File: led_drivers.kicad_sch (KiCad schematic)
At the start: 23 parts, among them IC1 SamacSys_Parts_HT16K33-28SOP, IC2 SamacSys_Parts_HT16K33-28SOP, SW1 SW_Alps_SKRK, SW2 SW_Alps_SKRK, SW3 SW_Omron_B3FS, SW4 SW_Alps_SKRK

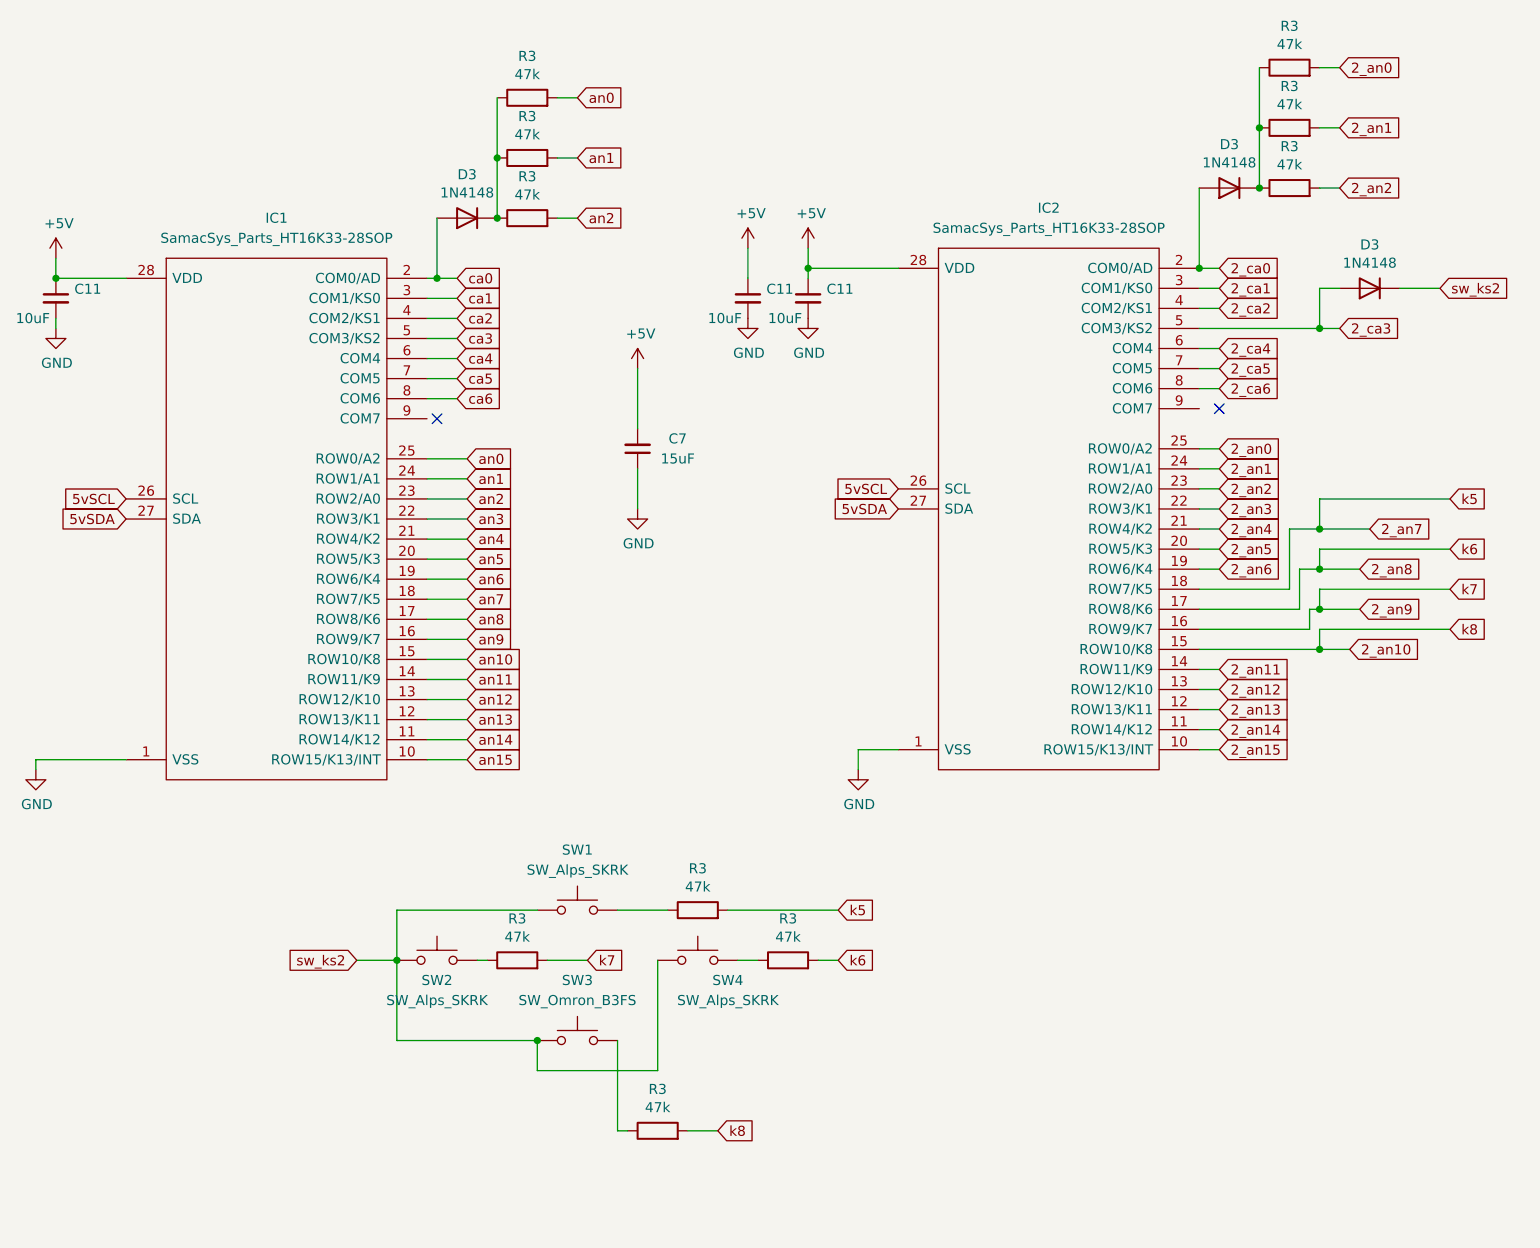
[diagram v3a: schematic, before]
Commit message: Change tactile shwitches
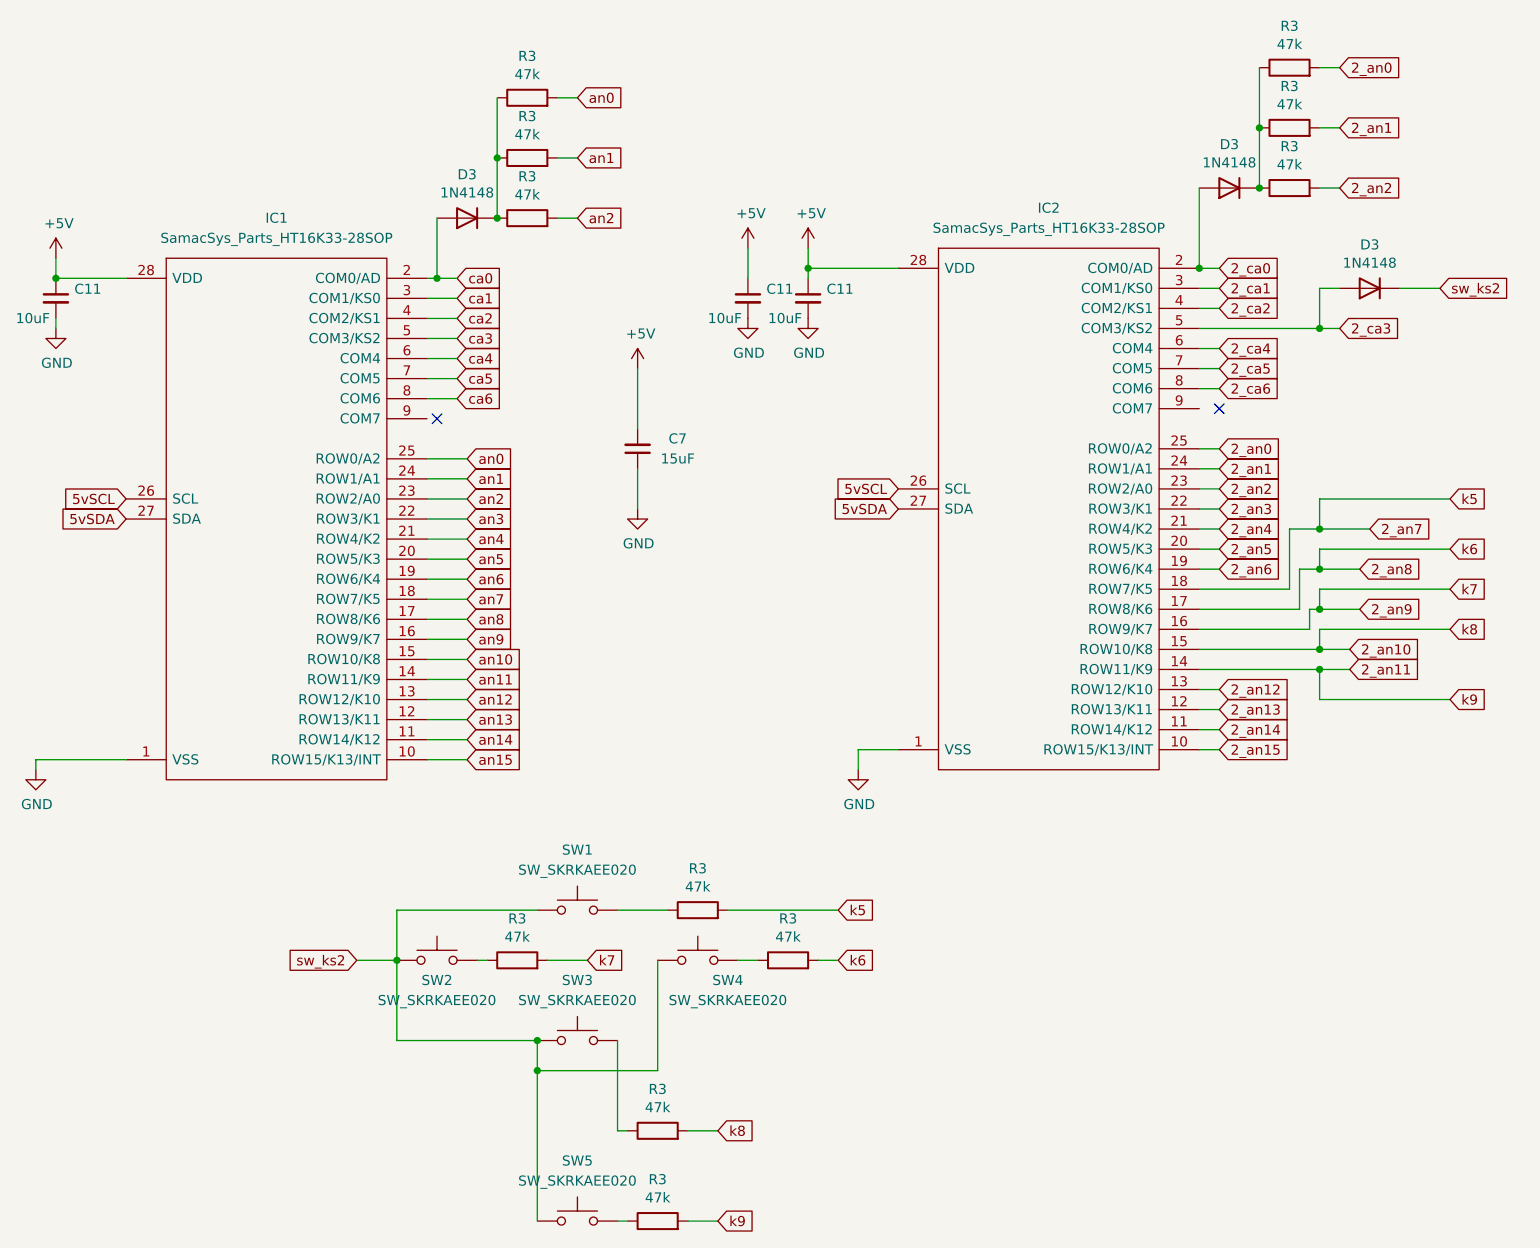
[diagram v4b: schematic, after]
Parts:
- added R3: 47k, Resistor_SMD:R_0603_1608Metric, symbol Device:R
- added SW5: SW_SKRKAEE020, Library:SKRKAEE020, symbol Switch:SW_Push
- SW1, SW2, SW4: value SW_Alps_SKRK -> SW_SKRKAEE020; footprint Button_Switch_SMD:SW_Push_SPST_NO_Alps_SKRK -> Library:SKRKAEE020
- SW3: value SW_Omron_B3FS -> SW_SKRKAEE020; footprint Button_Switch_SMD:SW_Push_SPST_NO_Alps_SKRK -> Library:SKRKAEE020
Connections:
- net 2_an11: now also R3.2
- net sw_ks2: now also SW5.1
- new net: R3.1, SW5.2
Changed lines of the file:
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@@
   (junction (at 205.74 90.17) (diameter 0) (color 0 0 0 0)
   )
+  (junction (at 205.74 102.87) (diameter 0) (color 0 0 0 0)
+  )
   (junction (at 93.98 53.34) (diameter 0) (color 0 0 0 0)
   )
@@
   )
   (junction (at 106.68 149.86) (diameter 0) (color 0 0 0 0)
+  )
+  (junction (at 106.68 153.67) (diameter 0) (color 0 0 0 0)
   )
   (no_connect (at 93.98 71.12))
@@
     (stroke (width 0) (type default))
   )
+  (wire (pts (xy 205.74 106.68) (xy 222.25 106.68))
+    (stroke (width 0) (type default))
+  )
   (wire (pts (xy 190.5 110.49) (xy 193.04 110.49))
     (stroke (width 0) (type default))
@@
     (stroke (width 0) (type default))
   )
+  (wire (pts (xy 116.84 172.72) (xy 118.11 172.72))
+    (stroke (width 0) (type default))
+  )
   (wire (pts (xy 205.74 81.28) (xy 205.74 85.09))
     (stroke (width 0) (type default))
@@
     (stroke (width 0) (type default))
   )
+  (wire (pts (xy 106.68 153.67) (xy 106.68 172.72))
+    (stroke (width 0) (type default))
+  )
   (wire (pts (xy 222.25 87.63) (xy 205.74 87.63))
     (stroke (width 0) (type default))
@@
     (stroke (width 0) (type default))
   )
+  (wire (pts (xy 205.74 106.68) (xy 205.74 102.87))
+    (stroke (width 0) (type default))
+  )
   (wire (pts (xy 152.4 52.07) (xy 140.97 52.07))
     (stroke (width 0) (type default))
@@
     (stroke (width 0) (type default))
   )
+  (wire (pts (xy 125.73 172.72) (xy 129.54 172.72))
+    (stroke (width 0) (type default))
+  )
   (wire (pts (xy 106.68 153.67) (xy 106.68 149.86))
     (stroke (width 0) (type default))
@@
     (stroke (width 0) (type default))
   )
-  (wire (pts (xy 190.5 102.87) (xy 193.04 102.87))
+  (wire (pts (xy 190.5 102.87) (xy 205.74 102.87))
     (stroke (width 0) (type default))
   )
@@
   )
   (wire (pts (xy 133.35 49.53) (xy 133.35 53.34))
+    (stroke (width 0) (type default))
+  )
+  (wire (pts (xy 205.74 102.87) (xy 209.55 102.87))
     (stroke (width 0) (type default))
   )
@@
     )
   )
-  (global_label "2_an11" (shape input) (at 193.04 102.87 0)
-    (effects (font (size 1.27 1.27)) (justify left))
-    (property "Intersheetrefs" "${INTERSHEET_REFS}" (at 193.04 102.87 0)
+  (global_label "2_an11" (shape input) (at 209.55 102.87 0)
+    (effects (font (size 1.27 1.27)) (justify left))
+    (property "Intersheetrefs" "${INTERSHEET_REFS}" (at 209.55 102.87 0)
       (effects (font (size 1.27 1.27)) hide)
     )
@@
     (effects (font (size 1.27 1.27)) (justify left))
     (property "Intersheetrefs" "${INTERSHEET_REFS}" (at 111.76 30.48 0)
+      (effects (font (size 1.27 1.27)) hide)
+    )
+  )
+  (global_label "k9" (shape input) (at 222.25 106.68 0)
+    (effects (font (size 1.27 1.27)) (justify left))
+    (property "Intersheetrefs" "${INTERSHEET_REFS}" (at 222.25 106.68 0)
       (effects (font (size 1.27 1.27)) hide)
     )
@@
     (effects (font (size 1.27 1.27)) (justify left))
     (property "Intersheetrefs" "${INTERSHEET_REFS}" (at 210.82 95.25 0)
+      (effects (font (size 1.27 1.27)) hide)
+    )
+  )
+  (global_label "k9" (shape input) (at 129.54 172.72 0)
+    (effects (font (size 1.27 1.27)) (justify left))
+    (property "Intersheetrefs" "${INTERSHEET_REFS}" (at 129.54 172.72 0)
       (effects (font (size 1.27 1.27)) hide)
     )
@@
       (effects (font (size 1.27 1.27)))
     )
-    (property "Value" "SW_Omron_B3FS" (at 111.76 144.78 0)
-      (effects (font (size 1.27 1.27)))
-    )
-    (property "Footprint" "Button_Switch_SMD:SW_Push_SPST_NO_Alps_SKRK" (at 111.76 144.78 0)
-      (effects (font (size 1.27 1.27)) hide)
-    )
-    (property "Datasheet" "" (at 111.76 144.78 0)
+    (property "Value" "SW_SKRKAEE020" (at 111.76 144.78 0)
+      (effects (font (size 1.27 1.27)))
+    )
+    (property "Footprint" "Library:SKRKAEE020" (at 111.76 144.78 0)
+      (effects (font (size 1.27 1.27)) hide)
+    )
+    (property "Datasheet" "https://www.mouser.ca/datasheet/2/15/SKRK-1370789.pdf" (at 111.76 144.78 0)
       (effects (font (size 1.27 1.27)) hide)
     )
@@
         (path "/eed35b77-cbf9-4596-9b17-2558f81058ba/7d22e16e-a0ba-4766-b1de-c8cbb28f14f7"
           (reference "SW3") (unit 1)
+        )
+      )
+    )
+  )
+  (symbol (lib_id "Switch:SW_Push") (at 111.76 172.72 0) (unit 1)
+    (in_bom yes) (on_board yes) (dnp no) (fields_autoplaced)
+    (property "Reference" "SW5" (at 111.76 165.1 0)
+      (effects (font (size 1.27 1.27)))
+    )
+    (property "Value" "SW_SKRKAEE020" (at 111.76 167.64 0)
+      (effects (font (size 1.27 1.27)))
+    )
+    (property "Footprint" "Library:SKRKAEE020" (at 111.76 167.64 0)
+      (effects (font (size 1.27 1.27)) hide)
+    )
+    (property "Datasheet" "https://www.mouser.ca/datasheet/2/15/SKRK-1370789.pdf" (at 111.76 167.64 0)
+      (effects (font (size 1.27 1.27)) hide)
+    )
+    (pin "1")
+    (pin "2")
+    (instances
+      (project "ltp_kikad"
+        (path "/eed35b77-cbf9-4596-9b17-2558f81058ba/7d22e16e-a0ba-4766-b1de-c8cbb28f14f7"
+          (reference "SW5") (unit 1)
         )
       )
@@
       (effects (font (size 1.27 1.27)))
     )
-    (property "Value" "SW_Alps_SKRK" (at 111.76 128.27 0)
-      (effects (font (size 1.27 1.27)))
-    )
-    (property "Footprint" "Button_Switch_SMD:SW_Push_SPST_NO_Alps_SKRK" (at 111.76 128.27 0)
-      (effects (font (size 1.27 1.27)) hide)
-    )
-    (property "Datasheet" "" (at 111.76 128.27 0)
+    (property "Value" "SW_SKRKAEE020" (at 111.76 128.27 0)
+      (effects (font (size 1.27 1.27)))
+    )
+    (property "Footprint" "Library:SKRKAEE020" (at 111.76 128.27 0)
+      (effects (font (size 1.27 1.27)) hide)
+    )
+    (property "Datasheet" "https://www.mouser.ca/datasheet/2/15/SKRK-1370789.pdf" (at 111.76 128.27 0)
       (effects (font (size 1.27 1.27)) hide)
     )
@@
       (effects (font (size 1.27 1.27)))
     )
-    (property "Value" "SW_Alps_SKRK" (at 130.81 144.78 0)
-      (effects (font (size 1.27 1.27)))
-    )
-    (property "Footprint" "Button_Switch_SMD:SW_Push_SPST_NO_Alps_SKRK" (at 127 134.62 0)
-      (effects (font (size 1.27 1.27)) hide)
-    )
-    (property "Datasheet" "" (at 127 134.62 0)
+    (property "Value" "SW_SKRKAEE020" (at 130.81 144.78 0)
+      (effects (font (size 1.27 1.27)))
+    )
+    (property "Footprint" "Library:SKRKAEE020" (at 127 134.62 0)
+      (effects (font (size 1.27 1.27)) hide)
+    )
+    (property "Datasheet" "https://www.mouser.ca/datasheet/2/15/SKRK-1370789.pdf" (at 127 134.62 0)
       (effects (font (size 1.27 1.27)) hide)
     )
@@
     )
   )
+  (symbol (lib_id "Device:R") (at 121.92 172.72 90) (unit 1)
+    (in_bom yes) (on_board yes) (dnp no)
+    (property "Reference" "R3" (at 121.92 167.4622 90)
+      (effects (font (size 1.27 1.27)))
+    )
+    (property "Value" "47k" (at 121.92 169.7736 90)
+      (effects (font (size 1.27 1.27)))
+    )
+    (property "Footprint" "Resistor_SMD:R_0603_1608Metric" (at 121.92 174.498 90)
+      (effects (font (size 1.27 1.27)) hide)
+    )
+    (property "Datasheet" "~" (at 121.92 172.72 0)
+      (effects (font (size 1.27 1.27)) hide)
+    )
+    (pin "1")
+    (pin "2")
+    (instances
+      (project "LTP305_ESP32_CLOCK"
+        (path "/c007e288-8439-49d9-bbdf-49724c34958c"
+          (reference "R3") (unit 1)
+        )
+      )
+      (project "ltp_kikad"
+        (path "/eed35b77-cbf9-4596-9b17-2558f81058ba"
+          (reference "R2") (unit 1)
+        )
+        (path "/eed35b77-cbf9-4596-9b17-2558f81058ba/7d22e16e-a0ba-4766-b1de-c8cbb28f14f7"
+          (reference "R16") (unit 1)
+        )
+      )
+    )
+  )
   (symbol (lib_id "Switch:SW_Omron_B3FS") (at 93.98 139.7 0) (unit 1)
     (in_bom yes) (on_board yes) (dnp no)
@@
       (effects (font (size 1.27 1.27)))
     )
-    (property "Value" "SW_Alps_SKRK" (at 93.98 144.78 0)
-      (effects (font (size 1.27 1.27)))
-    )
-    (property "Footprint" "Button_Switch_SMD:SW_Push_SPST_NO_Alps_SKRK" (at 93.98 134.62 0)
-      (effects (font (size 1.27 1.27)) hide)
-    )
-    (property "Datasheet" "https://omronfs.omron.com/en_US/ecb/products/pdf/en-b3fs.pdf" (at 93.98 134.62 0)
-      (effects (font (size 1.27 1.27)) hide)
-    )
+    (property "Value" "SW_SKRKAEE020" (at 93.98 144.78 0)
+      (effects (font (size 1.27 1.27)))
+    )
+    (property "Footprint" "Library:SKRKAEE020" (at 93.98 134.62 0)
+      (effects (font (size 1.27 1.27)) hide)
+    )
+    (property "Datasheet" "https://www.mouser.ca/datasheet/2/15/SKRK-1370789.pdf" (at 93.98 134.62 0)
+      (effects (font (size 1.27 1.27)) hide)
+    )

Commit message: Add title block
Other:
- company: (none) -> Andrew Tudoroi
- title: (none) -> Pitanga HAT
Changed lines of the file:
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@@
 (kicad_sch (version 20230121) (generator eeschema)
   (paper "A4")
+  (title_block
+    (title "Pitanga HAT")
+    (date "2023-10-20")
+    (rev "2.1")
+    (company "Andrew Tudoroi")
+  )
   (junction (at 101.6 45.72) (diameter 0) (color 0 0 0 0)
   )
